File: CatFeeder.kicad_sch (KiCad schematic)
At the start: 40 parts, among them J1 B2B-XH-A(LF)(SN), J10 B2B-XH-A(LF)(SN), J11 B2B-XH-A(LF)(SN), J2 B3B-XH-A(LF)(SN), J3 Barrel_Jack, J4 B4B-XH-A(LF)(SN), J5 Conn_01x08_Female, J6 Conn_01x08_Female, J7 B2B-XH-A(LF)(SN), J8 B2B-XH-A(LF)(SN), J9 B2B-XH-A(LF)(SN), Q1 Q_NPN_BEC, Q2 Q_NPN_BEC, U1 SN74LVC1T45DBV, U2 LM2586SX-ADJ/NOPB_1, U3 DRV8871DDA

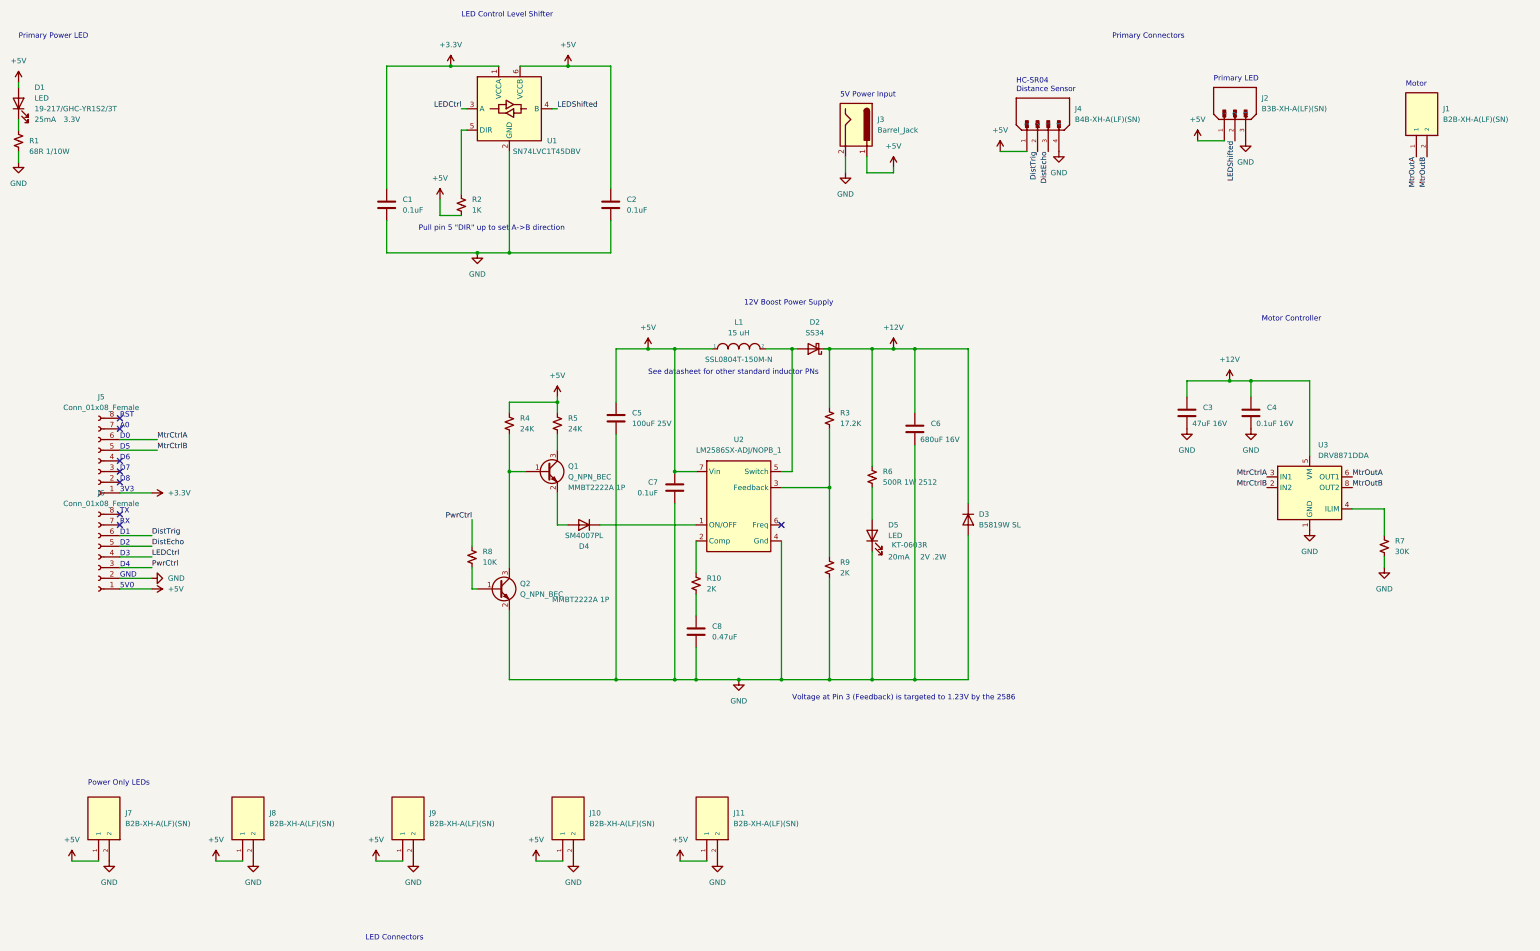
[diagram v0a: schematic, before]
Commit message: Added power plane to top layer, fixed some layout errors
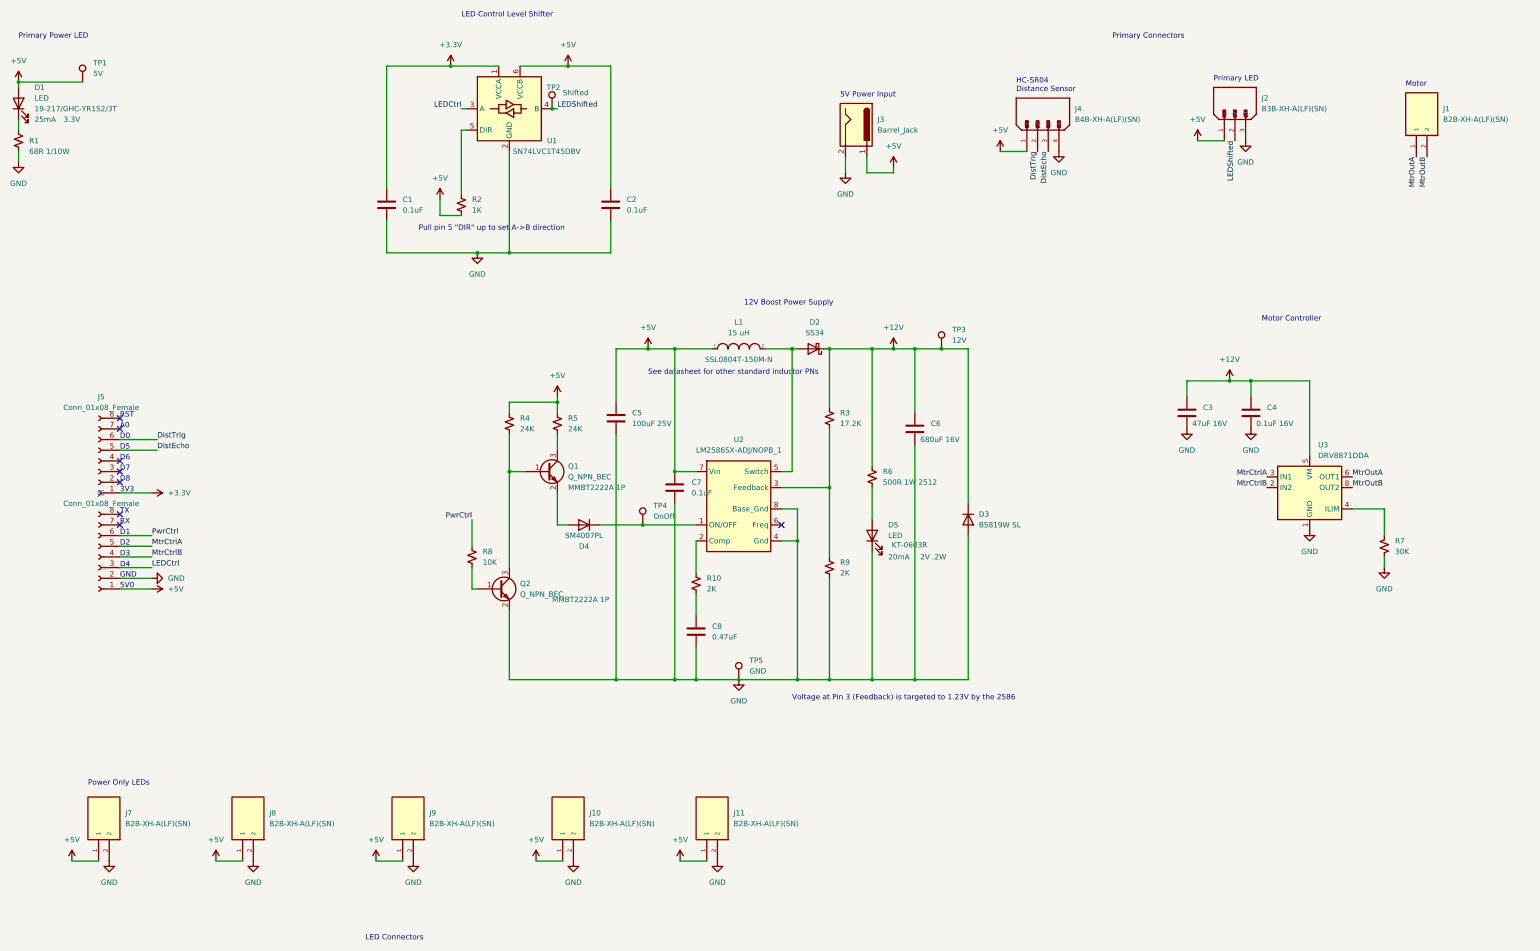
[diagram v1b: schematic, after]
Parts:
- added TP1: 5V, TestPoint:TestPoint_Pad_D1.5mm, symbol Connector:TestPoint
- added TP2: Shifted, TestPoint:TestPoint_Pad_D1.5mm, symbol Connector:TestPoint
- added TP3: 12V, TestPoint:TestPoint_Pad_D1.5mm, symbol Connector:TestPoint
- added TP4: OnOff, TestPoint:TestPoint_Pad_D1.0mm, symbol Connector:TestPoint
- added TP5: GND, TestPoint:TestPoint_Pad_D1.5mm, symbol Connector:TestPoint
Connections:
- net +12V: now also TP3.1
- net +5V: now also TP1.1
- net DistEcho: now also J5.5 (Pin_5); no longer J6.5 (Pin_5)
- net DistTrig: now also J5.6 (Pin_6); no longer J6.6 (Pin_6)
- net GND: now also U2.8 (Base_Gnd), TP5.1
- net LEDCtrl: now also J6.3 (Pin_3); no longer J6.4 (Pin_4)
- net LEDShifted: now also TP2.1
- net MtrCtrlA: now also J6.5 (Pin_5); no longer J5.6 (Pin_6)
- net MtrCtrlB: now also J6.4 (Pin_4); no longer J5.5 (Pin_5)
- net PwrCtrl: now also J6.6 (Pin_6); no longer J6.3 (Pin_3)
- net at D4.1 (K), U2.1 (ON/OFF): now also TP4.1

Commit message: Add pull ups to signals, tweak layout, reduce board size, add mounting holes
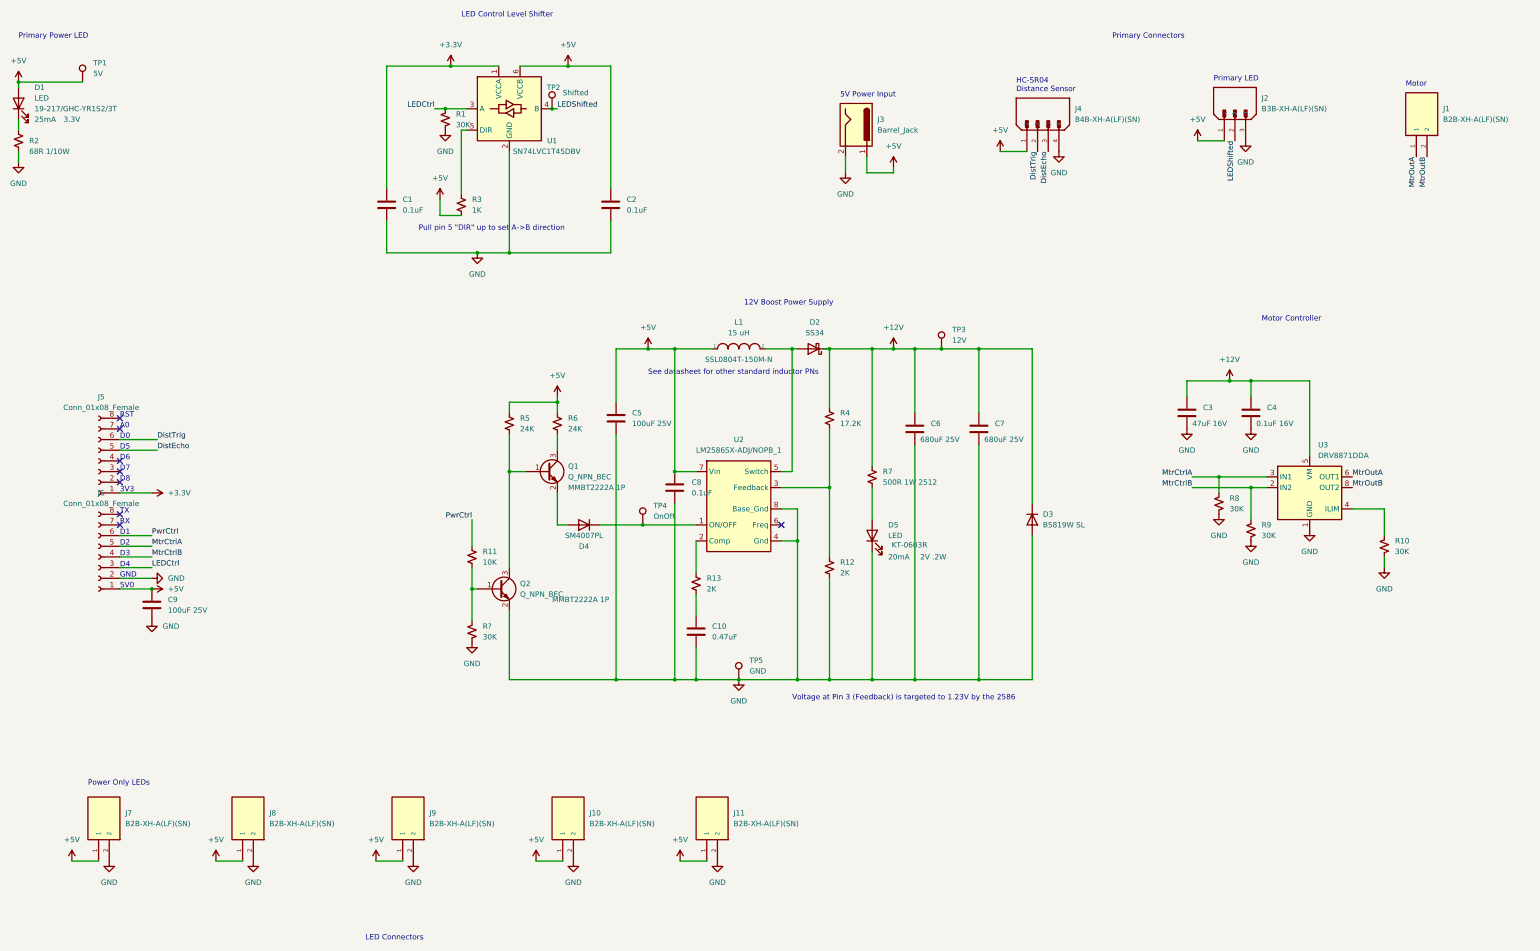
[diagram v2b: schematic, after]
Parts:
- added C7: 680uF 25V, Capacitor_THT:CP_Radial_D8.0mm_P3.50mm, symbol Device:C
- added C9: 100uF 25V, Capacitor_THT:CP_Radial_D8.0mm_P3.50mm, symbol Device:C
- added R1, R8, R9, R?: 30K, Resistor_SMD:R_0402_1005Metric, symbol Device:R_Small_US
- C6: value 680uF 16V -> 680uF 25V; PN KM681M016F115A -> SPE1EM681F16OL
- renumbered C8 to C10, C7 to C8, R7 to R10, R8 to R11, R9 to R12, R10 to R13, R1 to R2, R2 to R3, R3 to R4, R4 to R5, R5 to R6, R6 to R7
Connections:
- net +12V: now also C7.1
- net +5V: now also C9.1
- net GND: now also C7.2, C9.2, R1.2, R8.2, R9.2, R?.2
- net LEDCtrl: now also R1.1
- net MtrCtrlA: now also R8.1
- net MtrCtrlB: now also R9.1
- net at Q2.1 (B), R11.2: now also R?.1
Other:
- moved on the sheet: D3

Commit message: added series resistor for neopixel control line, layout improvements, changed suspect resistors to 0805 for easier future rework
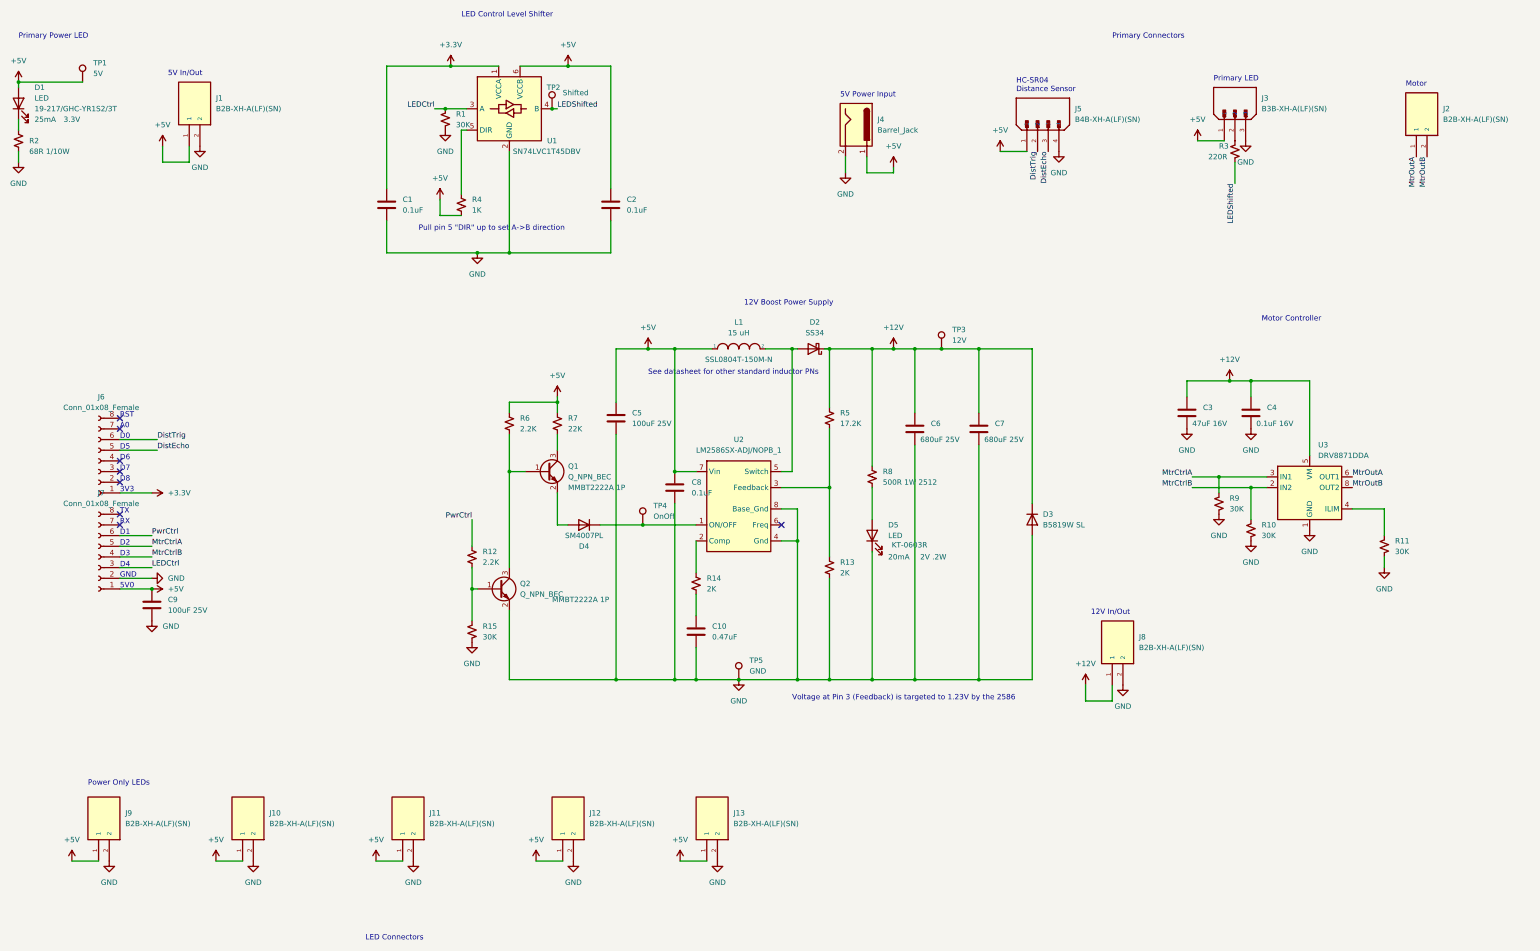
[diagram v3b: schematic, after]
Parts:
- removed R5: 24K, Resistor_SMD:R_0402_1005Metric, symbol Device:R_Small_US
- added J1, J8: B2B-XH-A(LF)(SN), Connector_JST:JST_XH_B2B-XH-A_1x02_P2.50mm_Vertical, symbol MarlinLib:B2B-XH-A(LF)(SN)
- added R3: 220R, Resistor_SMD:R_0805_2012Metric, symbol Device:R_Small_US
- added R6: 2.2K, Resistor_SMD:R_0805_2012Metric, symbol Device:R_Small_US
- R12: renamed from R11; value 10K -> 2.2K; footprint Resistor_SMD:R_0402_1005Metric -> Resistor_SMD:R_0805_2012Metric; PN 0402WGF1002TCE -> 0805W8F2201T5E
- R7: renamed from R6; value 24K -> 22K; footprint Resistor_SMD:R_0402_1005Metric -> Resistor_SMD:R_0805_2012Metric; PN 0402WGF2402TCE -> 0805W8F2202T5E
- gave numbers to parts that had none: 1
- renumbered J8 to J10, J9 to J11, J10 to J12, J11 to J13, J1 to J2, J2 to J3, J3 to J4, J4 to J5, J5 to J6, J6 to J7, J7 to J9, R9 to R10, R10 to R11, R12 to R13, R13 to R14, R3 to R4, R4 to R5, R7 to R8, R8 to R9
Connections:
- net +12V: now also J8.1
- net +5V: now also J1.1, R6.1
- net GND: now also J1.2, J8.2
- net LEDShifted: now also R3.2; no longer J3.2
- net at Q1.1 (B), Q2.3 (C): now also R6.2
- new net: J3.2, R3.1
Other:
- note added: "12V In/Out"
- note added: "5V In/Out"
